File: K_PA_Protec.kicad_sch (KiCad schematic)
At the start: 89 parts, among them IC1 MCP23017_SO, J1 IDC 10 Straight, J10 MH2, J11 MH3, J12 MH4, J13 MH5, J14 MH6, J2 Molex KK 4, J3 IDC 10 Straight, J4 Molex KK 2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

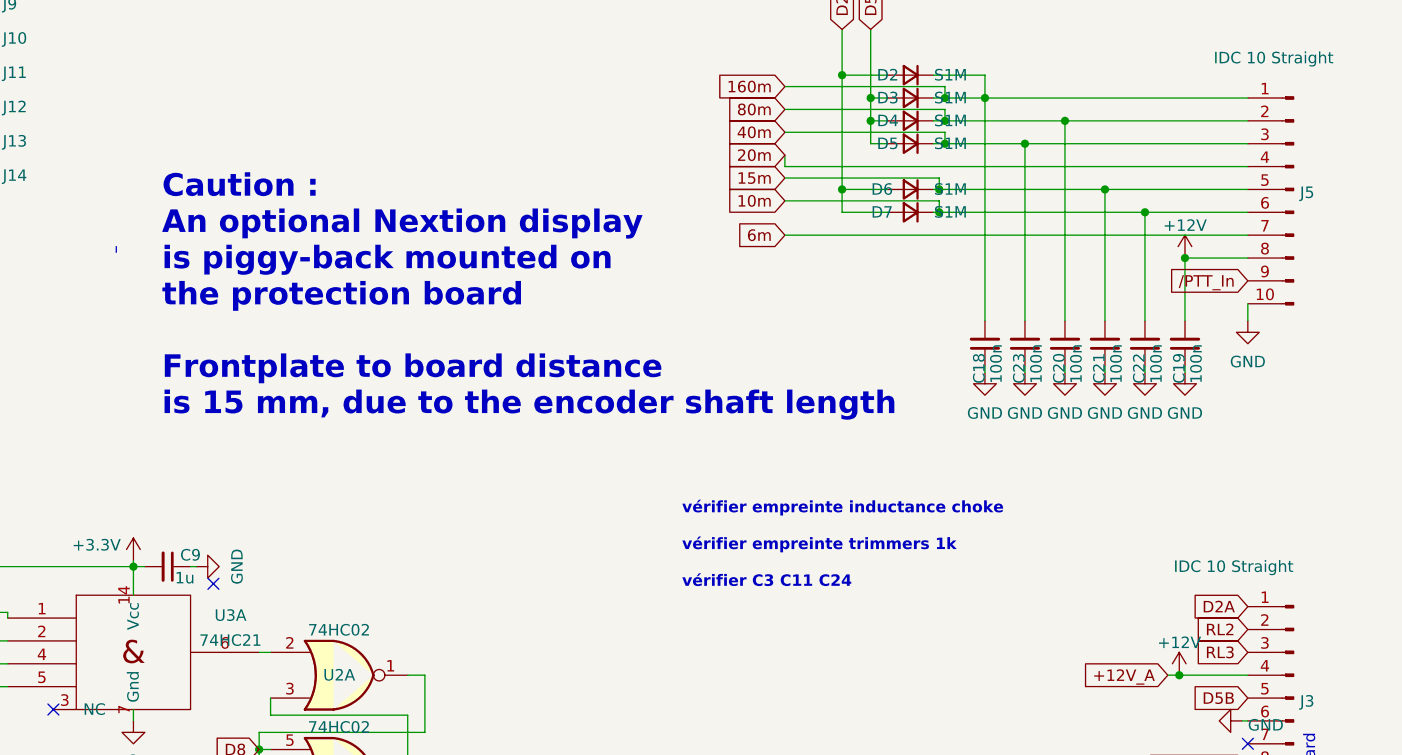
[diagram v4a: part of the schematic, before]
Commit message: nextion mounting holes fixed, last release before proto
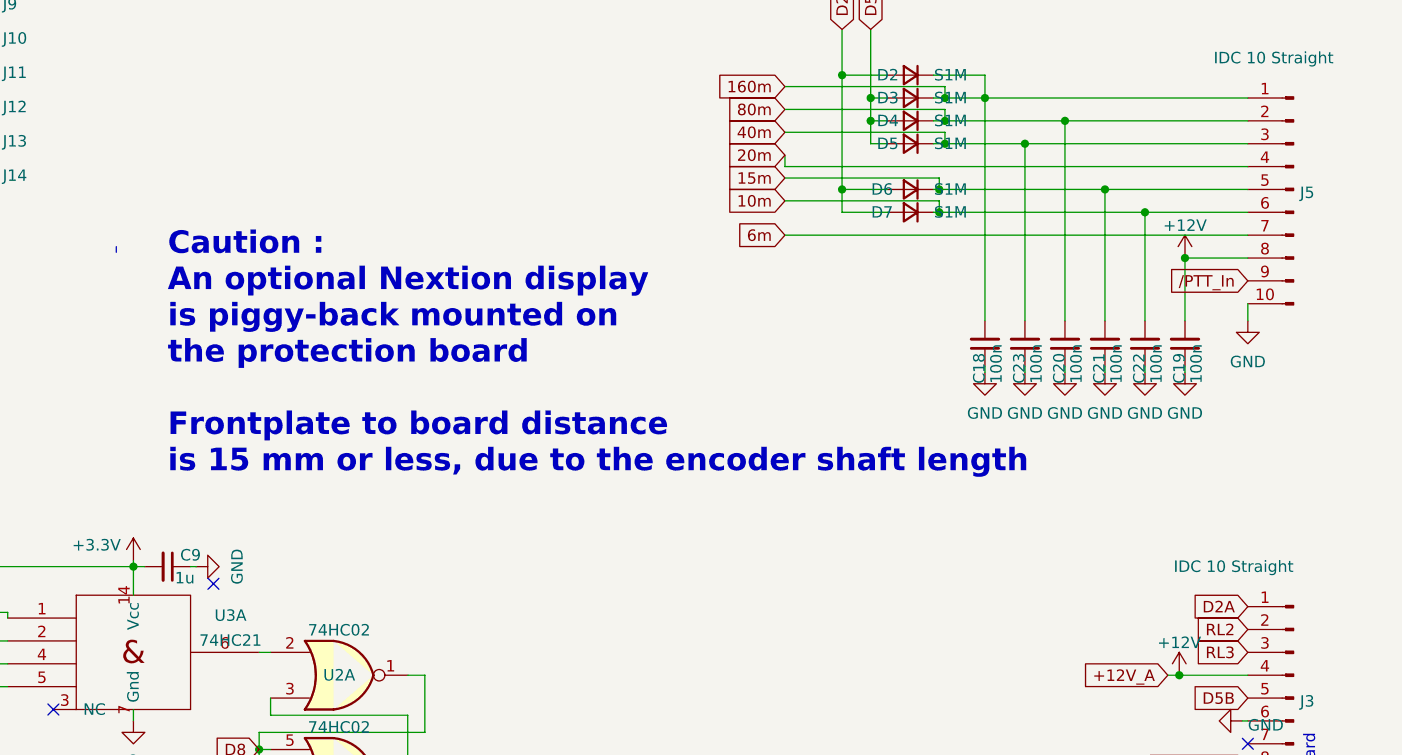
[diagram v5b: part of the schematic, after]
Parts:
- L1, L2, L3, L4: footprint Inductor_SMD:L_2512_6332Metric_Pad1.52x3.35mm_HandSolder -> Fair-Rite_2743021447:Fair-Rite_2743021447
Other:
- note added: "Caution : An optional Nextion display is piggy-back mounted on the protection board Frontplate to board distance is 15 mm or less, due to the encoder shaft length"
- note removed: "Caution : An optional Nextion display is piggy-back mounted on the protection board Frontplate to board distance is 15 mm, due to the encoder shaft length"
- note removed: "vérifier empreinte inductance choke vérifier empreinte trimmers 1k vérifier C3 C11 C24"
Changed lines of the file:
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@@
     (effects (font (size 1.27 1.27) bold) (justify left bottom))
   )
-  (text "Caution : \nAn optional Nextion display \nis piggy-back mounted on\nthe protection board\n\nFrontplate to board distance \nis 15 mm, due to the encoder shaft length \n"
-    (at 156.21 62.865 0)
+  (text "Caution : \nAn optional Nextion display \nis piggy-back mounted on\nthe protection board\n\nFrontplate to board distance \nis 15 mm or less, due to the encoder shaft length \n"
+    (at 156.845 69.215 0)
     (effects (font (size 2.5 2.5) (thickness 0.5) bold) (justify left bottom))
   )
@@
     (effects (font (size 1.27 1.27)) (justify left bottom))
   )
-  (text "vérifier empreinte inductance choke\n\nvérifier empreinte trimmers 1k\n\nvérifier C3 C11 C24"
-    (at 213.995 81.915 0)
-    (effects (font (size 1.27 1.27) bold) (justify left bottom))
-  )
   (global_label "RL3" (shape input) (at 212.725 132.715 0) (fields_autoplaced)
     (effects (font (size 1.27 1.27)) (justify left))
@@
     (property "Reference" "L2" (id 0) (at 35.56 57.15 90))
     (property "Value" "2743021447" (id 1) (at 34.29 55.245 90))
-    (property "Footprint" "Inductor_SMD:L_2512_6332Metric_Pad1.52x3.35mm_HandSolder" (id 2) (at 38.735 60.198 90)
+    (property "Footprint" "Fair-Rite_2743021447:Fair-Rite_2743021447" (id 2) (at 38.735 60.198 90)
       (effects (font (size 1.27 1.27)) hide)
     )
@@
     (property "Reference" "L3" (id 0) (at 66.675 62.865 90))
     (property "Value" "2743021447" (id 1) (at 64.77 67.945 90))
-    (property "Footprint" "Inductor_SMD:L_2512_6332Metric_Pad1.52x3.35mm_HandSolder" (id 2) (at 69.215 65.913 90)
+    (property "Footprint" "Fair-Rite_2743021447:Fair-Rite_2743021447" (id 2) (at 69.215 65.913 90)
       (effects (font (size 1.27 1.27)) hide)
     )
@@
     (property "Reference" "L4" (id 0) (at 36.195 62.865 90))
     (property "Value" "2743021447" (id 1) (at 35.56 66.04 90))
-    (property "Footprint" "Inductor_SMD:L_2512_6332Metric_Pad1.52x3.35mm_HandSolder" (id 2) (at 38.735 65.278 90)
+    (property "Footprint" "Fair-Rite_2743021447:Fair-Rite_2743021447" (id 2) (at 38.735 65.278 90)
       (effects (font (size 1.27 1.27)) hide)
     )
@@
     (property "Reference" "L1" (id 0) (at 66.675 57.15 90))
     (property "Value" "2743021447" (id 1) (at 69.1769 55.5268 90))
-    (property "Footprint" "Inductor_SMD:L_2512_6332Metric_Pad1.52x3.35mm_HandSolder" (id 2) (at 69.215 60.198 90)
+    (property "Footprint" "Fair-Rite_2743021447:Fair-Rite_2743021447" (id 2) (at 69.215 60.198 90)
       (effects (font (size 1.27 1.27)) hide)
     )
@@
     )
     (path "/cba67685-7297-4a97-9b38-4424ffaae1ce"
-      (reference "L1") (unit 1) (value "2743021447") (footprint "Inductor_SMD:L_2512_6332Metric_Pad1.52x3.35mm_HandSolder")
+      (reference "L1") (unit 1) (value "2743021447") (footprint "Fair-Rite_2743021447:Fair-Rite_2743021447")
     )
     (path "/0afa5357-c57e-42cd-b476-72d99f39fe9f"
-      (reference "L2") (unit 1) (value "2743021447") (footprint "Inductor_SMD:L_2512_6332Metric_Pad1.52x3.35mm_HandSolder")
+      (reference "L2") (unit 1) (value "2743021447") (footprint "Fair-Rite_2743021447:Fair-Rite_2743021447")
     )
     (path "/14f06a7d-ac78-4907-9c78-b5c7e405269b"
-      (reference "L3") (unit 1) (value "2743021447") (footprint "Inductor_SMD:L_2512_6332Metric_Pad1.52x3.35mm_HandSolder")
+      (reference "L3") (unit 1) (value "2743021447") (footprint "Fair-Rite_2743021447:Fair-Rite_2743021447")
     )
     (path "/542cea8d-aff9-4b40-a7cb-e44a542a6722"
-      (reference "L4") (unit 1) (value "2743021447") (footprint "Inductor_SMD:L_2512_6332Metric_Pad1.52x3.35mm_HandSolder")
+      (reference "L4") (unit 1) (value "2743021447") (footprint "Fair-Rite_2743021447:Fair-Rite_2743021447")
     )
     (path "/32026461-ff43-45e2-b343-8b73e4507a73"

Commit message: minor changes in the README file
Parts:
- J8: value Molex KK 4 -> 12V out
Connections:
- net GND: now also J7.2 (Pin_2); no longer J7.3 (Pin_3)
- net at C15.2, J7.1 (Pin_1), L2.1: now also J7.3 (Pin_3)
- no-connect marks 16 -> 15
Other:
- note added: "Caution : An optional Nextion VSWR display is piggy-back mounted on the protection board Frontplate to board distance is 15 mm or less, due to the encoder shaft length"
- note added: "From I/O Board"
- note added: "Main Power In (warning : not the LA2NI order)"
- note added: "PA PROTECTION BOARD, Kicad V.6.0 version 1.0 Design : Eng. LA2NI 23/09/2022 first draft 24/01/2021"
- note added: "To Aries ATU"
- note added: "to Aries ATU encoder in J 18"
- note added: "to Aries ATU pwr in"
- note removed: "Caution : An optional Nextion display is piggy-back mounted on the protection board Frontplate to board distance is 15 mm or less, due to the encoder shaft length"
- note removed: "PA PROTECTION BOARD, Kicad version 1.0 Design : Eng. LA2NI 23/09/2022 first draft 24/01/2021"
- moved on the sheet: J7
